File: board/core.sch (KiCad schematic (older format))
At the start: 14 parts, among them U4 ATSAML21E18B-AUT, Y1 HC49S

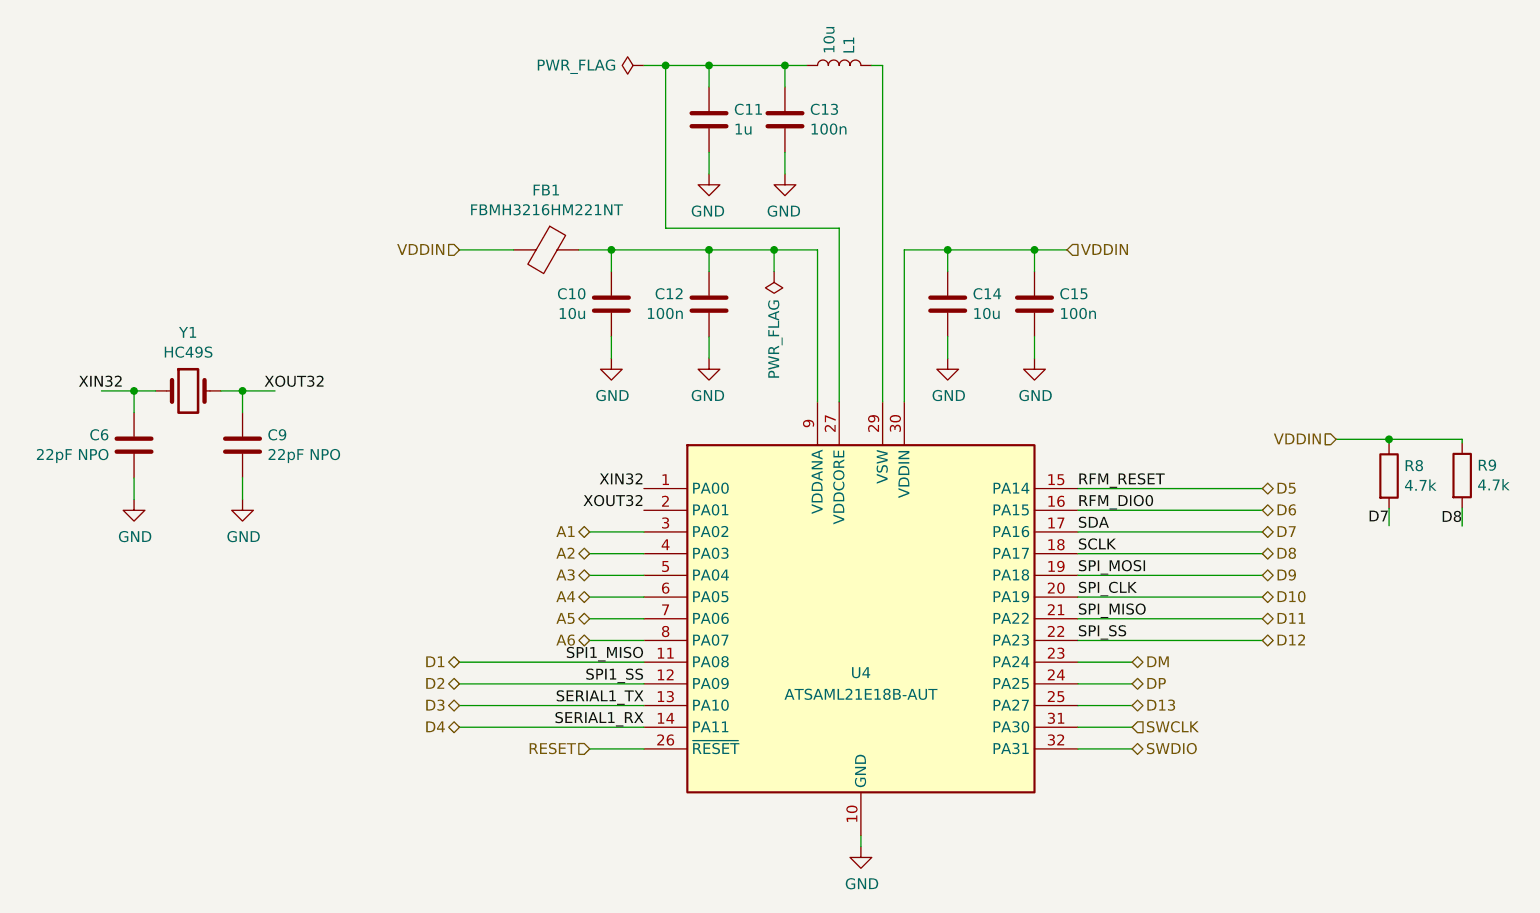
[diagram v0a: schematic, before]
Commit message: Changes to the board to prepare for RC1
- Added pull-down R (10k)
- Changed XTAL (ABS10)
- Changed values for load caps (C7-9) for XTAL
- Changed PROG value for batt controller (2k)
- Updated pin headers to include 3v3 and RFM_DIO1 pins
- Added jumpers to disable voltage divider (1M) on pin A6
- Repositioned USB connector, components and labels

Sign-off: LFRM, 03-23-2021
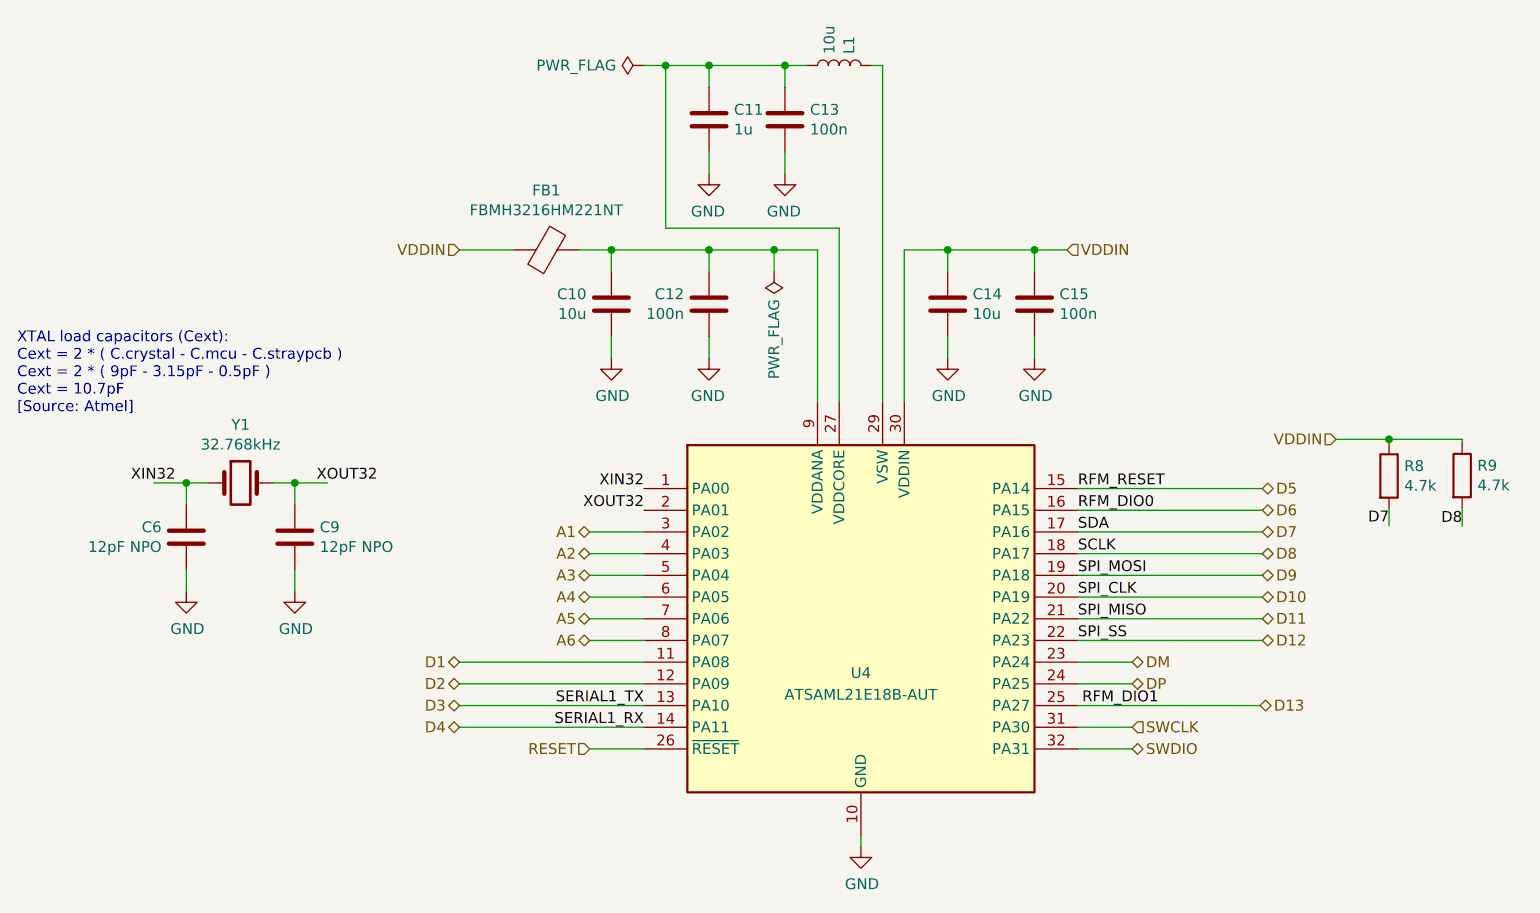
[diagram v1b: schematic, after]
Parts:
- C6, C9: value 22pF NPO -> 12pF NPO
- Y1: value HC49S -> 32.768kHz; footprint Crystal:Crystal_HC49-U_Vertical -> Crystal:Crystal_SMD_MicroCrystal_CC4V-T1A-2Pin_5.0x1.9mm_HandSoldering
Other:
- note added: "XTAL load capacitors (Cext):\nCext = 2 * ( C.crystal - C.mcu - C.straypcb )\nCext = 2 * ( 9pF - 3.15pF - 0.5pF )\nCext = 10.7pF\n[Source: Atmel]"
- moved on the sheet: C6, C9, Y1
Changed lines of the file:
@@
 	7150 4100 8000 4100
-Wire Wire Line
-	7150 4600 7400 4600
 Wire Wire Line
 	7150 4200 8000 4200
@@
 Text HLabel 7400 4500 2    50   BiDi ~ 0
 DP
-Text HLabel 7400 4600 2    50   BiDi ~ 0
+Text HLabel 7990 4600 2    50   BiDi ~ 0
 D13
 Wire Wire Line
@@
 Text Label 5150 4600 2    50   ~ 0
 SERIAL1_TX
-Text Label 5150 4500 2    50   ~ 0
-SPI1_SS
-Text Label 5150 4400 2    50   ~ 0
-SPI1_MISO
+Text Label 7521 4600 2    50   ~ 0
+RFM_DIO1
 Text Label 7150 4100 0    50   ~ 0
 SPI_CLK
@@
 Text HLabel 8340 3373 0    50   Input ~ 0
 VDDIN
-Text Label 3400 3150 0    50   ~ 0
+Text Label 3641 3574 0    50   ~ 0
 XOUT32
 Wire Wire Line
-	2800 3150 2900 3150
-Wire Wire Line
-	2800 3250 2800 3150
-Wire Wire Line
-	3300 3150 3200 3150
-Wire Wire Line
-	3300 3250 3300 3150
+	3041 3574 3141 3574
+Wire Wire Line
+	3041 3674 3041 3574
+Wire Wire Line
+	3541 3574 3441 3574
+Wire Wire Line
+	3541 3674 3541 3574
 $Comp
 L Device:C C?
 U 1 1 5F3C031F
-P 2800 3400
+P 3041 3824
 AR Path="/5F3C031F" Ref="C?"  Part="1"
 AR Path="/5F3BBDAE/5F3C031F" Ref="C6"  Part="1"
-F 0 "C6" H 2686 3354 50  0000 R CNN
-F 1 "22pF NPO" H 2686 3445 50  0000 R CNN
-F 2 "Capacitor_SMD:C_1206_3216Metric_Pad1.33x1.80mm_HandSolder" H 2838 3250 50  0001 C CNN
-F 3 "~" H 2800 3400 50  0001 C CNN
-	1    2800 3400
+F 0 "C6" H 2927 3778 50  0000 R CNN
+F 1 "12pF NPO" H 2927 3869 50  0000 R CNN
+F 2 "Capacitor_SMD:C_1206_3216Metric_Pad1.33x1.80mm_HandSolder" H 3079 3674 50  0001 C CNN
+F 3 "~" H 3041 3824 50  0001 C CNN
+	1    3041 3824
 	1    0    0    1
 $EndComp
@@
 L Device:C C?
 U 1 1 5F3C0319
-P 3300 3400
+P 3541 3824
 AR Path="/5F3C0319" Ref="C?"  Part="1"
 AR Path="/5F3BBDAE/5F3C0319" Ref="C9"  Part="1"
-F 0 "C9" H 3185 3354 50  0000 R CNN
-F 1 "22pF NPO" H 3185 3445 50  0000 R CNN
-F 2 "Capacitor_SMD:C_1206_3216Metric_Pad1.33x1.80mm_HandSolder" H 3338 3250 50  0001 C CNN
-F 3 "~" H 3300 3400 50  0001 C CNN
-	1    3300 3400
+F 0 "C9" H 3426 3778 50  0000 R CNN
+F 1 "12pF NPO" H 3426 3869 50  0000 R CNN
+F 2 "Capacitor_SMD:C_1206_3216Metric_Pad1.33x1.80mm_HandSolder" H 3579 3674 50  0001 C CNN
+F 3 "~" H 3541 3824 50  0001 C CNN
+	1    3541 3824
 	-1   0    0    1
 $EndComp
@@
 L Device:Crystal Y?
 U 1 1 5F3C0313
-P 3050 3150
+P 3291 3574
 AR Path="/5F3C0313" Ref="Y?"  Part="1"
 AR Path="/5F3BBDAE/5F3C0313" Ref="Y1"  Part="1"
-F 0 "Y1" H 3050 3418 50  0000 C CNN
-F 1 "HC49S" H 3050 3327 50  0000 C CNN
-F 2 "Crystal:Crystal_HC49-U_Vertical" H 3050 3150 50  0001 C CNN
-F 3 "~" H 3050 3150 50  0001 C CNN
-	1    3050 3150
-	1    0    0    -1
-$EndComp
-Wire Wire Line
-	3300 3150 3450 3150
-Connection ~ 3300 3150
+F 0 "Y1" H 3291 3842 50  0000 C CNN
+F 1 "32.768kHz" H 3291 3751 50  0000 C CNN
+F 2 "Crystal:Crystal_SMD_MicroCrystal_CC4V-T1A-2Pin_5.0x1.9mm_HandSoldering" H 3291 3574 50  0001 C CNN
+F 3 "~" H 3291 3574 50  0001 C CNN
+	1    3291 3574
+	1    0    0    -1
+$EndComp
+Wire Wire Line
+	3541 3574 3691 3574
+Connection ~ 3541 3574
 $Comp
 L power:GND #PWR?
 U 1 1 5F3C0329
-P 2800 3650
+P 3041 4074
 AR Path="/5F3C0329" Ref="#PWR?"  Part="1"
 AR Path="/5F3BBDAE/5F3C0329" Ref="#PWR026"  Part="1"
-F 0 "#PWR026" H 2800 3400 50  0001 C CNN
-F 1 "GND" H 2805 3477 50  0000 C CNN
-F 2 "" H 2800 3650 50  0001 C CNN
-F 3 "" H 2800 3650 50  0001 C CNN
-	1    2800 3650
-	1    0    0    -1
-$EndComp
-Wire Wire Line
-	2800 3650 2800 3550
+F 0 "#PWR026" H 3041 3824 50  0001 C CNN
+F 1 "GND" H 3046 3901 50  0000 C CNN
+F 2 "" H 3041 4074 50  0001 C CNN
+F 3 "" H 3041 4074 50  0001 C CNN
+	1    3041 4074
+	1    0    0    -1
+$EndComp
+Wire Wire Line
+	3041 4074 3041 3974
 $Comp
 L power:GND #PWR?
 U 1 1 5F3C0337
-P 3300 3650
+P 3541 4074
 AR Path="/5F3C0337" Ref="#PWR?"  Part="1"
 AR Path="/5F3BBDAE/5F3C0337" Ref="#PWR030"  Part="1"
-F 0 "#PWR030" H 3300 3400 50  0001 C CNN
-F 1 "GND" H 3305 3477 50  0000 C CNN
-F 2 "" H 3300 3650 50  0001 C CNN
-F 3 "" H 3300 3650 50  0001 C CNN
-	1    3300 3650
-	1    0    0    -1
-$EndComp
-Wire Wire Line
-	3300 3650 3300 3550
-Text Label 2750 3150 2    50   ~ 0
+F 0 "#PWR030" H 3541 3824 50  0001 C CNN
+F 1 "GND" H 3546 3901 50  0000 C CNN
+F 2 "" H 3541 4074 50  0001 C CNN
+F 3 "" H 3541 4074 50  0001 C CNN
+	1    3541 4074
+	1    0    0    -1
+$EndComp
+Wire Wire Line
+	3541 4074 3541 3974
+Text Label 2991 3574 2    50   ~ 0
 XIN32
-Connection ~ 2800 3150
-Wire Wire Line
-	2800 3150 2650 3150
+Connection ~ 3041 3574
+Wire Wire Line
+	3041 3574 2891 3574
+Wire Wire Line
+	7150 4600 7990 4600
+Text Notes 2261 3259 0    50   ~ 0
+XTAL load capacitors (Cext):\nCext = 2 * ( C.crystal - C.mcu - C.straypcb )\nCext = 2 * ( 9pF - 3.15pF - 0.5pF )\nCext = 10.7pF\n[Source: Atmel]
 $EndSCHEMATC

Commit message: Pending fixes on rc1:
- added 10u cap for batt controller
- fixed poor connections on schematic, missed traces on D1 and C7
- changed RFMDIO1 pin to D1 (fixes issues w/ LoRa downlink)
- realigned components, repositioned traces
- increased pad sizes for hand-solderability on Q1 and U2
- overall retracing and re-alignment of components

Sign-off: LFRM, 07-03-2021
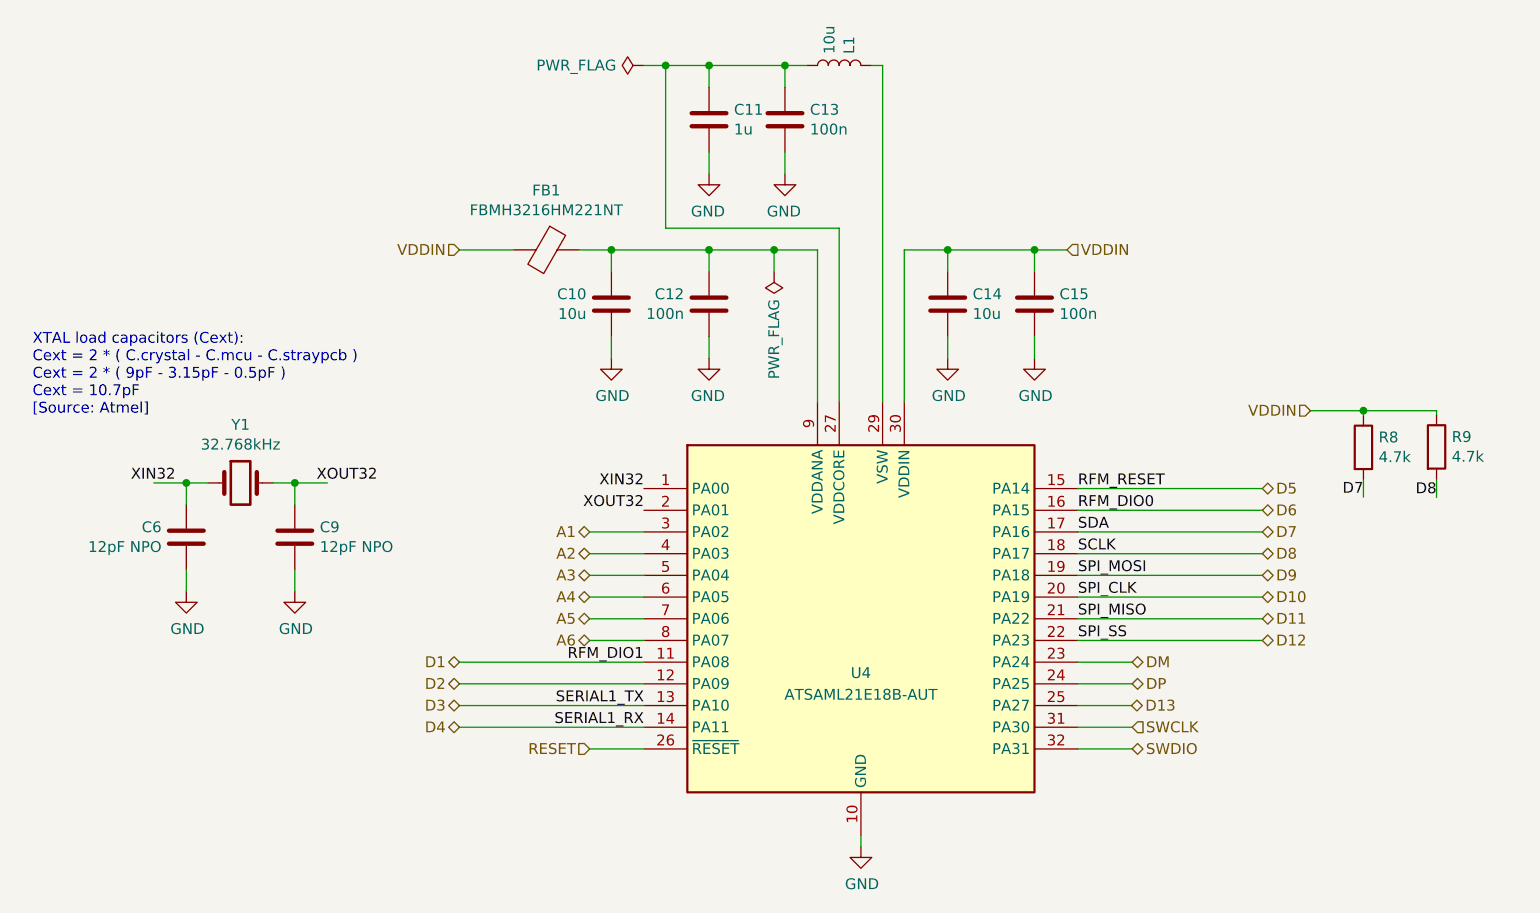
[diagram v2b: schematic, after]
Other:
- moved on the sheet: R8, R9
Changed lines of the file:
@@
 Text HLabel 7400 4500 2    50   BiDi ~ 0
 DP
-Text HLabel 7990 4600 2    50   BiDi ~ 0
+Text HLabel 7397 4600 2    50   BiDi ~ 0
 D13
 Wire Wire Line
@@
 Text Label 5150 4600 2    50   ~ 0
 SERIAL1_TX
-Text Label 7521 4600 2    50   ~ 0
+Text Label 5149 4400 2    50   ~ 0
 RFM_DIO1
 Text Label 7150 4100 0    50   ~ 0
@@
 L Device:R R8
 U 1 1 60EA4304
-P 8584 3542
-F 0 "R8" H 8654 3588 50  0000 L CNN
-F 1 "4.7k" H 8654 3497 50  0000 L CNN
-F 2 "Resistor_SMD:R_1206_3216Metric_Pad1.30x1.75mm_HandSolder" V 8514 3542 50  0001 C CNN
-F 3 "~" H 8584 3542 50  0001 C CNN
-	1    8584 3542
+P 8466 3410
+F 0 "R8" H 8536 3456 50  0000 L CNN
+F 1 "4.7k" H 8536 3365 50  0000 L CNN
+F 2 "Resistor_SMD:R_1206_3216Metric_Pad1.30x1.75mm_HandSolder" V 8396 3410 50  0001 C CNN
+F 3 "~" H 8466 3410 50  0001 C CNN
+	1    8466 3410
 	1    0    0    -1
 $EndComp
@@
 L Device:R R9
 U 1 1 60EA4845
-P 8921 3540
-F 0 "R9" H 8991 3586 50  0000 L CNN
-F 1 "4.7k" H 8991 3495 50  0000 L CNN
-F 2 "Resistor_SMD:R_1206_3216Metric_Pad1.30x1.75mm_HandSolder" V 8851 3540 50  0001 C CNN
-F 3 "~" H 8921 3540 50  0001 C CNN
-	1    8921 3540
-	1    0    0    -1
-$EndComp
-Wire Wire Line
-	8921 3373 8921 3390
-Wire Wire Line
-	8340 3373 8584 3373
-Wire Wire Line
-	8584 3392 8584 3373
-Connection ~ 8584 3373
-Wire Wire Line
-	8584 3373 8921 3373
-Wire Wire Line
-	8584 3692 8584 3771
-Wire Wire Line
-	8921 3690 8921 3773
-Text Label 8584 3771 2    50   ~ 0
+P 8803 3408
+F 0 "R9" H 8873 3454 50  0000 L CNN
+F 1 "4.7k" H 8873 3363 50  0000 L CNN
+F 2 "Resistor_SMD:R_1206_3216Metric_Pad1.30x1.75mm_HandSolder" V 8733 3408 50  0001 C CNN
+F 3 "~" H 8803 3408 50  0001 C CNN
+	1    8803 3408
+	1    0    0    -1
+$EndComp
+Wire Wire Line
+	8803 3241 8803 3258
+Wire Wire Line
+	8222 3241 8466 3241
+Wire Wire Line
+	8466 3260 8466 3241
+Connection ~ 8466 3241
+Wire Wire Line
+	8466 3241 8803 3241
+Wire Wire Line
+	8466 3560 8466 3639
+Wire Wire Line
+	8803 3558 8803 3641
+Text Label 8466 3639 2    50   ~ 0
 D7
-Text Label 8921 3773 2    50   ~ 0
+Text Label 8803 3641 2    50   ~ 0
 D8
-Text HLabel 8340 3373 0    50   Input ~ 0
+Text HLabel 8222 3241 0    50   Input ~ 0
 VDDIN
 Text Label 3641 3574 0    50   ~ 0
@@
 Wire Wire Line
 	3041 3574 2891 3574
-Wire Wire Line
-	7150 4600 7990 4600
-Text Notes 2261 3259 0    50   ~ 0
+Text Notes 2332 3266 0    50   ~ 0
 XTAL load capacitors (Cext):\nCext = 2 * ( C.crystal - C.mcu - C.straypcb )\nCext = 2 * ( 9pF - 3.15pF - 0.5pF )\nCext = 10.7pF\n[Source: Atmel]
+Wire Wire Line
+	7150 4600 7397 4600
 $EndSCHEMATC
